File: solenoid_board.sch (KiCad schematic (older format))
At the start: 31 parts, among them J1 Screw_Terminal_01x02, J10 Screw_Terminal_01x02, J11 Screw_Terminal_01x02, J12 Screw_Terminal_01x06, J13 Conn_01x01_Male, J2 MCU_LEFT_LEGS, J3 MCU_RIGHT_LEGS, J4 Solenoid_PWR_Supply, J5 RJ45, J6 Screw_Terminal_01x06, J7 Screw_Terminal_01x02, J8 Screw_Terminal_01x02, J9 Screw_Terminal_01x02, Q1 PHP79NQ08LT, Q2 PHP79NQ08LT, Q3 PHP79NQ08LT, Q4 PHP79NQ08LT, Q5 PHP79NQ08LT, Q6 PHP79NQ08LT, U1 CDSOT23-SM712, U4 SN65HVD72DR, U5 74HC165, U6 74HC165

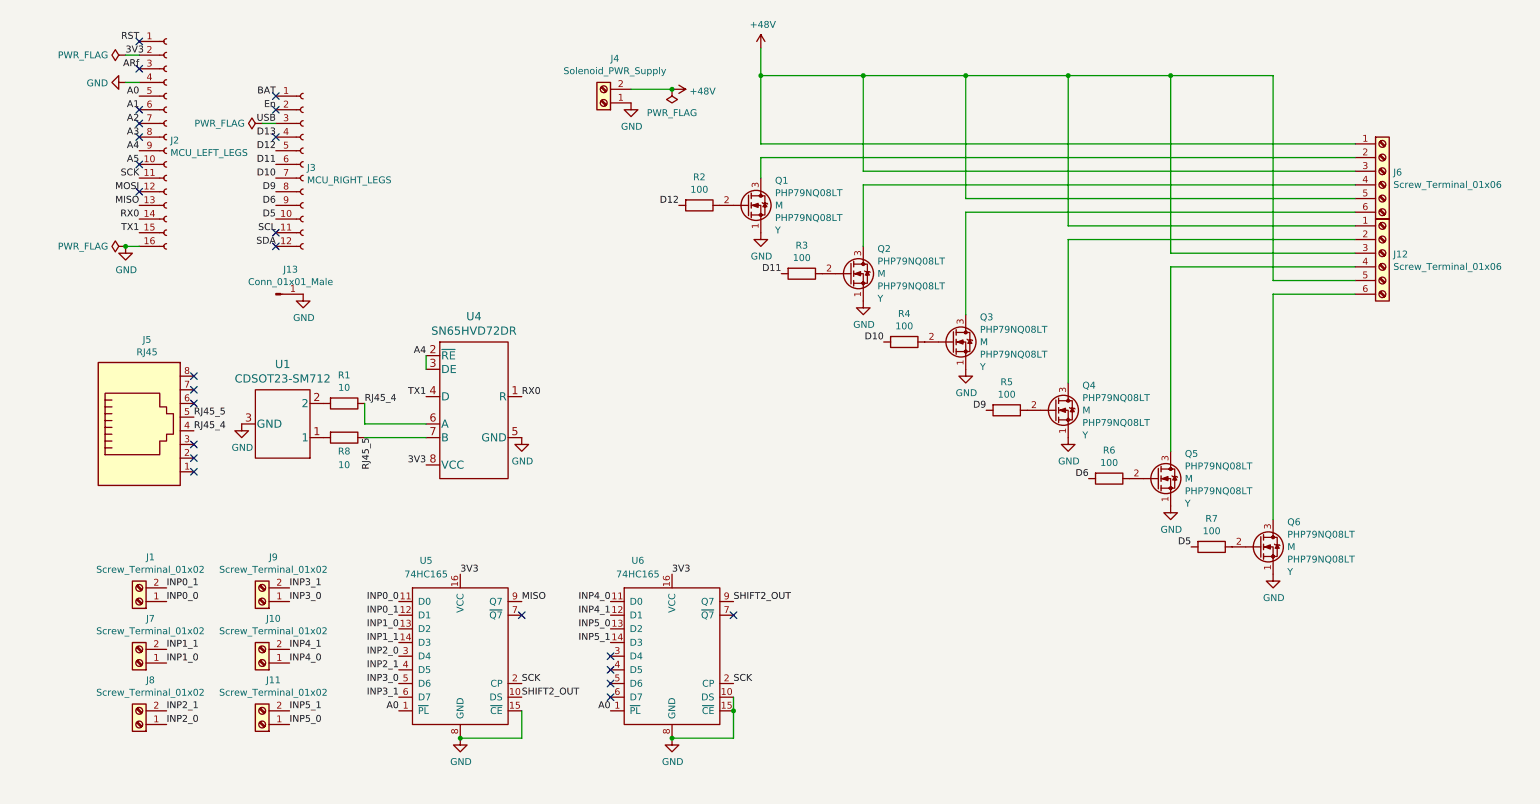
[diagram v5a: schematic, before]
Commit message: Stylistic Changes to clean up the Schematic. Added a +5 V screw terminal input to power the MCU. Switched the Shift Registers from +3.3V to +5 V supply, as is typical according to the datasheet. Added 12 +3.3V outputs to power the periphery.
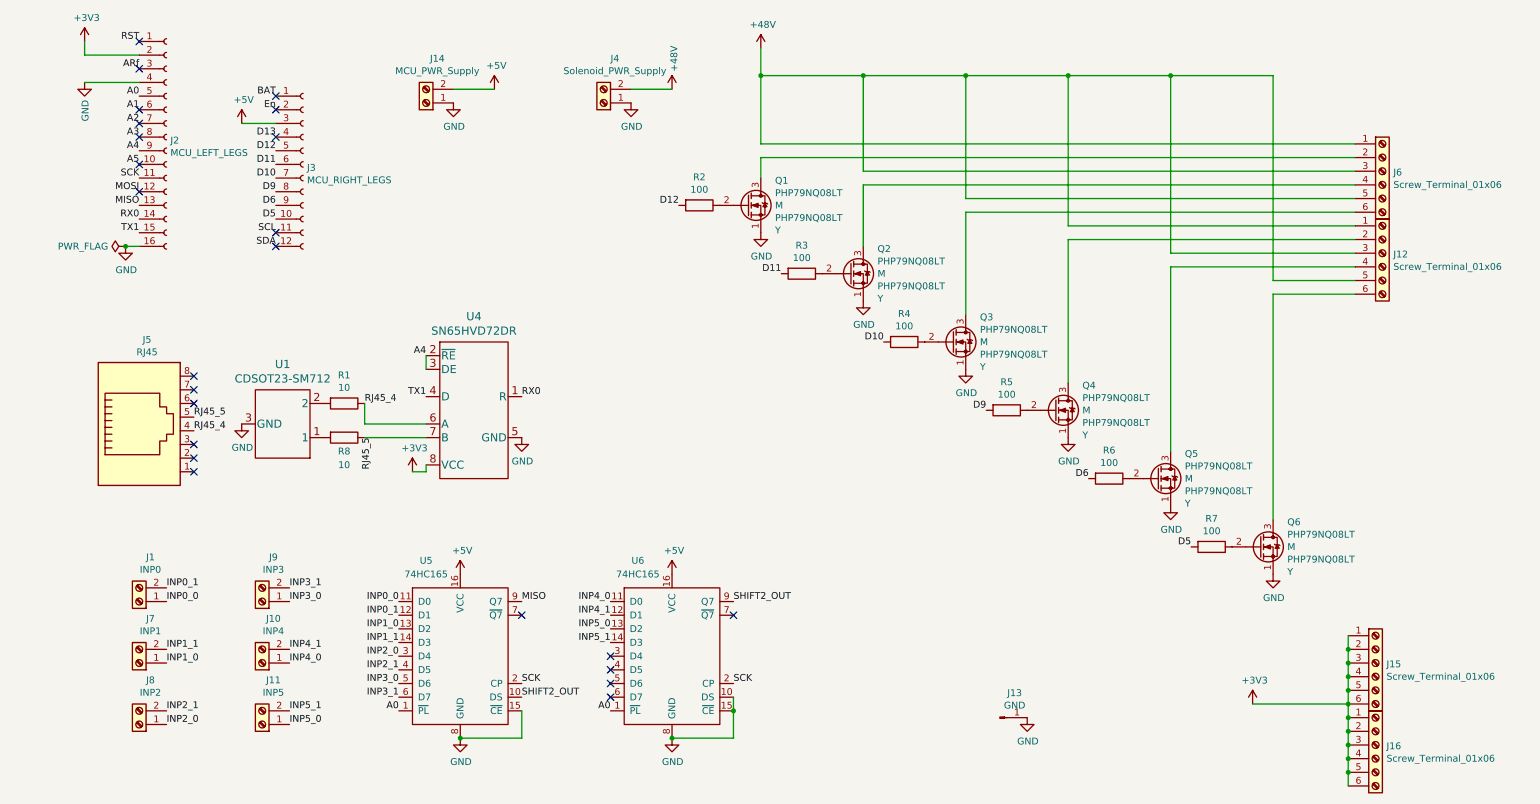
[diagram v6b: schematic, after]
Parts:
- added J14: MCU_PWR_Supply, TerminalBlock:TerminalBlock_bornier-2_P5.08mm, symbol Connector:Screw_Terminal_01x02
- added J15, J16: Screw_Terminal_01x06, TerminalBlock:TerminalBlock_bornier-6_P5.08mm, symbol Connector:Screw_Terminal_01x06
- J1: value Screw_Terminal_01x02 -> INP0
- J10: value Screw_Terminal_01x02 -> INP4
- J11: value Screw_Terminal_01x02 -> INP5
- J13: value Conn_01x01_Male -> GND
- J7: value Screw_Terminal_01x02 -> INP1
- J8: value Screw_Terminal_01x02 -> INP2
- J9: value Screw_Terminal_01x02 -> INP3
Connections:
- net GND: now also J14.1 (Pin_1)
- net 3V3 renamed +3V3
- net +3V3: now also J15.1 (Pin_1), J15.2 (Pin_2), J15.3 (Pin_3), J15.4 (Pin_4), J15.5 (Pin_5), J15.6 (Pin_6), J16.1 (Pin_1), J16.2 (Pin_2), J16.3 (Pin_3), J16.4 (Pin_4), J16.5 (Pin_5), J16.6 (Pin_6); no longer U5.16 (VCC), U6.16 (VCC)
- net USB renamed +5V
- net +5V: now also U5.16 (VCC), U6.16 (VCC), J14.2 (Pin_2)
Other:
- moved on the sheet: J13

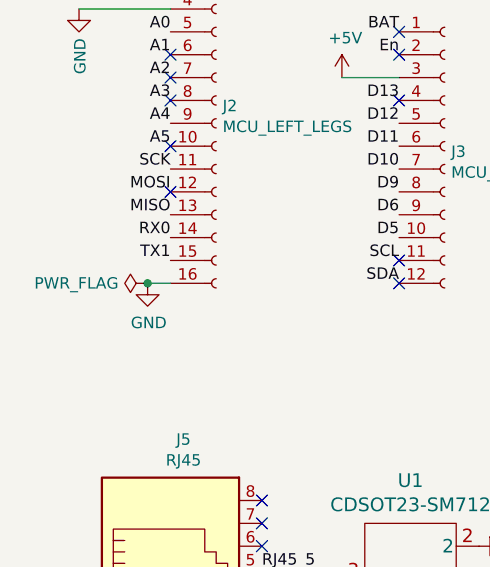
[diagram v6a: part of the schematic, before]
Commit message: Removed last PWR_FLAG to make schematic cleaner
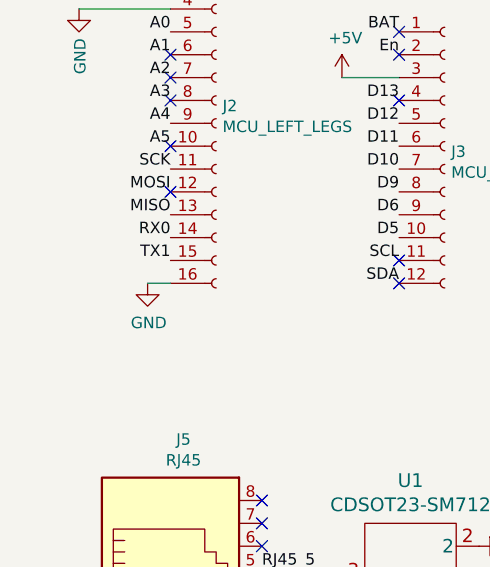
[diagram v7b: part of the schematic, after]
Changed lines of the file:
@@
 	4000 5800 3550 5800
 Connection ~ 3550 5800
-$Comp
-L power:PWR_FLAG #FLG0103
-U 1 1 5E13D366
-P 1100 2200
-F 0 "#FLG0103" H 1100 2275 50  0001 C CNN
-F 1 "PWR_FLAG" V 1100 2327 50  0000 L CNN
-F 2 "" H 1100 2200 50  0001 C CNN
-F 3 "~" H 1100 2200 50  0001 C CNN
-	1    1100 2200
-	0    -1   -1   0
-$EndComp
-Connection ~ 1100 2200
 Wire Wire Line
 	4800 1050 5100 1050

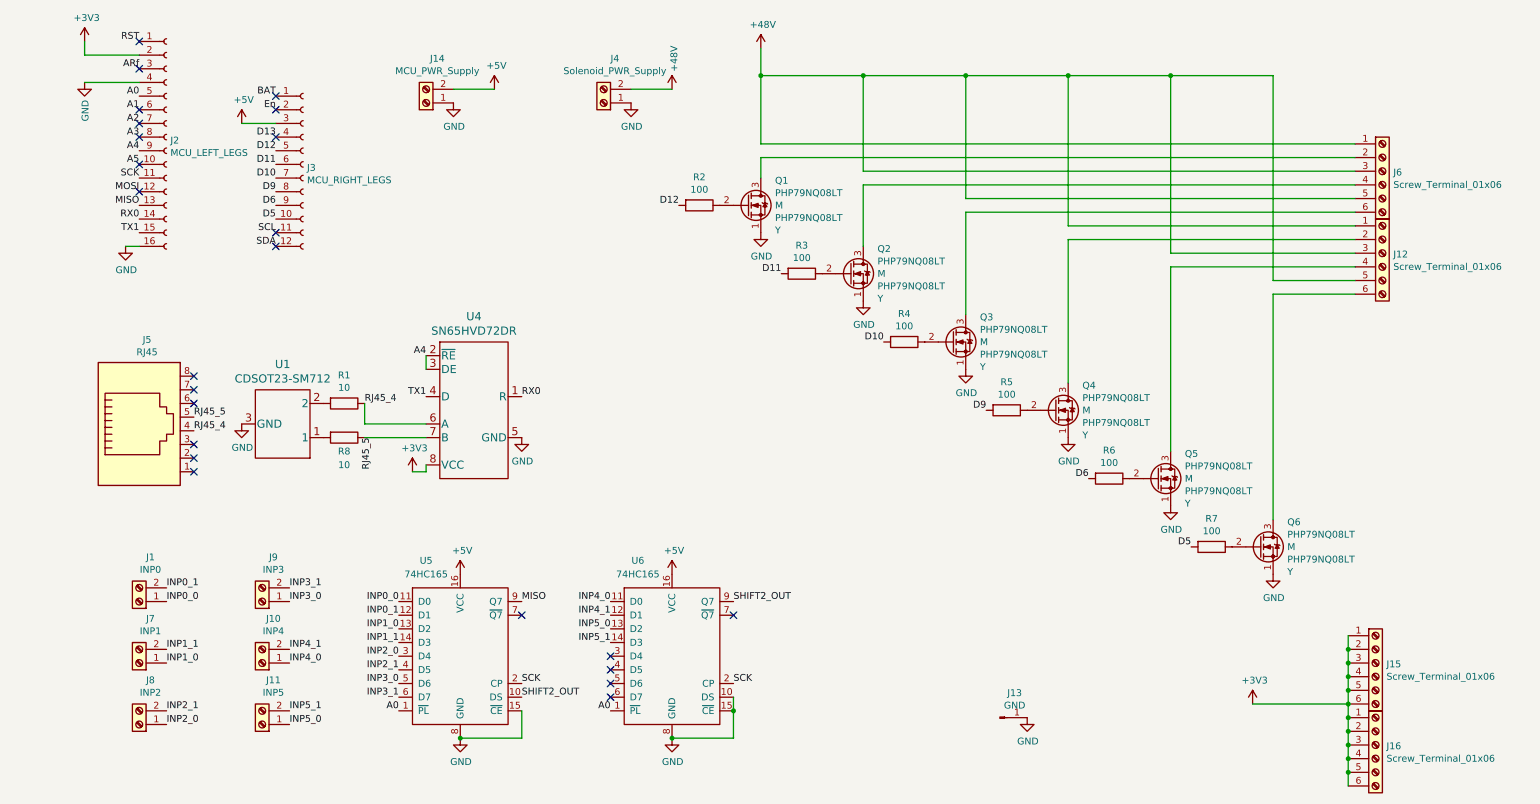
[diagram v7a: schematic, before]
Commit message: Cleaned up Schematic Reference Values - These will be printed on PCB and will make post-production soldering easier. Deleted and remade the layout to start with a clean slate on geometry with the newly added objects.
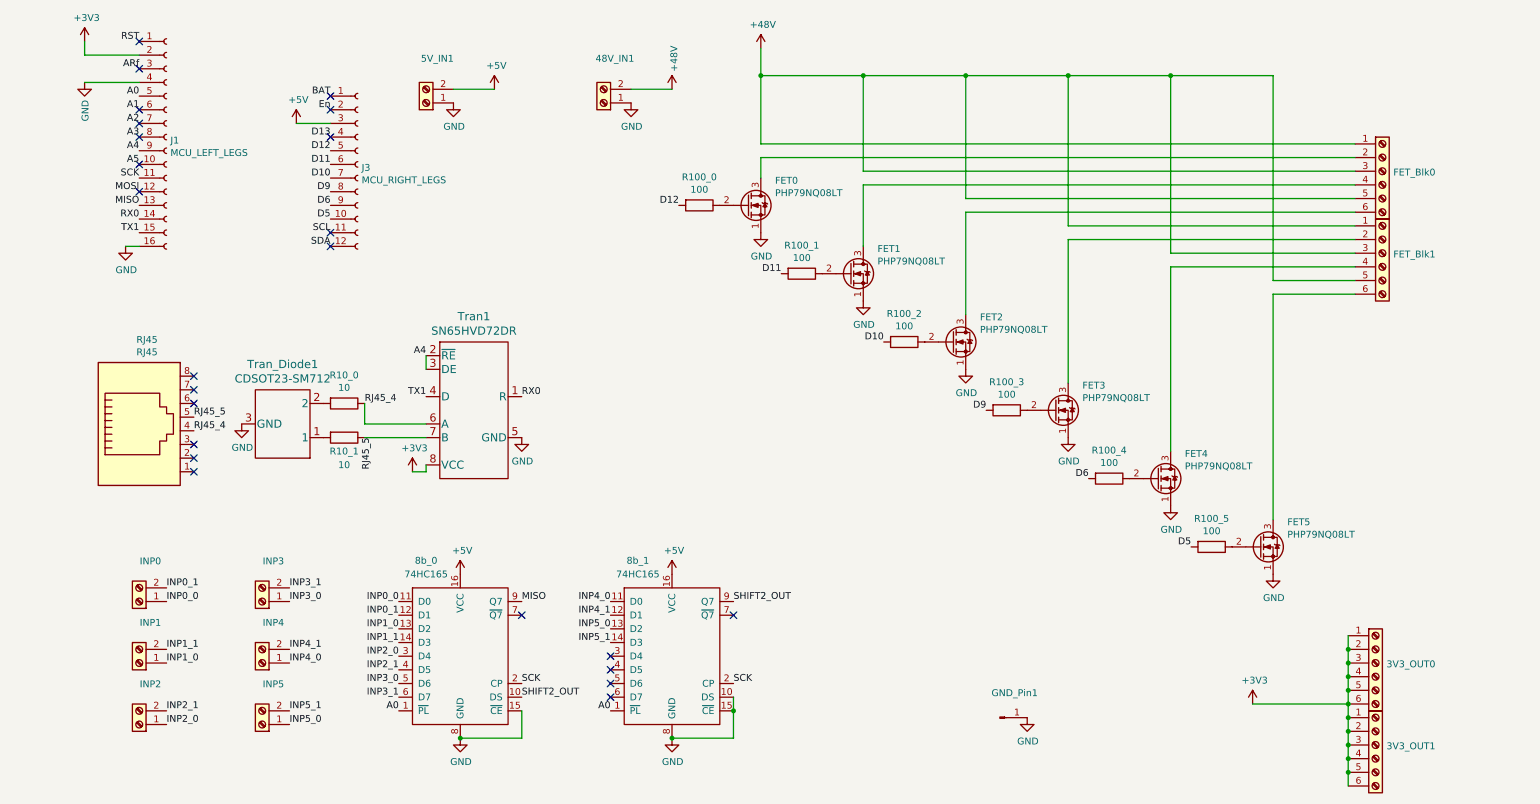
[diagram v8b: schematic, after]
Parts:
- 48V_IN1: renamed from J4; value Solenoid_PWR_Supply -> Screw_Terminal_01x02
- 5V_IN1: renamed from J14; value MCU_PWR_Supply -> Screw_Terminal_01x02
- INP0: renamed from J1; value INP0 -> Screw_Terminal_01x02
- INP1: renamed from J7; value INP1 -> Screw_Terminal_01x02
- INP2: renamed from J8; value INP2 -> Screw_Terminal_01x02
- INP3: renamed from J9; value INP3 -> Screw_Terminal_01x02
- INP4: renamed from J10; value INP4 -> Screw_Terminal_01x02
- INP5: renamed from J11; value INP5 -> Screw_Terminal_01x02
- renumbered J15 to 3V3_OUT0, J16 to 3V3_OUT1, U5 to 8b_0, U6 to 8b_1, Q1 to FET0, Q2 to FET1, Q3 to FET2, Q4 to FET3, Q5 to FET4, Q6 to FET5, J6 to FET_Blk0, J12 to FET_Blk1, J13 to GND_Pin1, J2 to J1, R2 to R100_0, R3 to R100_1, R4 to R100_2, R5 to R100_3, R6 to R100_4, R7 to R100_5, R1 to R10_0, R8 to R10_1, J5 to RJ45, U4 to Tran1, U1 to Tran_Diode1
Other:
- moved on the sheet: J3
